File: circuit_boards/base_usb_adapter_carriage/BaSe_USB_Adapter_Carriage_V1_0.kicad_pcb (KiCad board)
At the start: 4 copper layers, 38.8 x 33.4 mm, 15 parts, among them J1 USB_C_Receptacle, J3 USB3_A, J4 Screw_Terminal_01x03, J5 Screw_Terminal_01x03, J6 Conn_01x03, J7 USB3_B_Micro, P1 USB_C_Plug

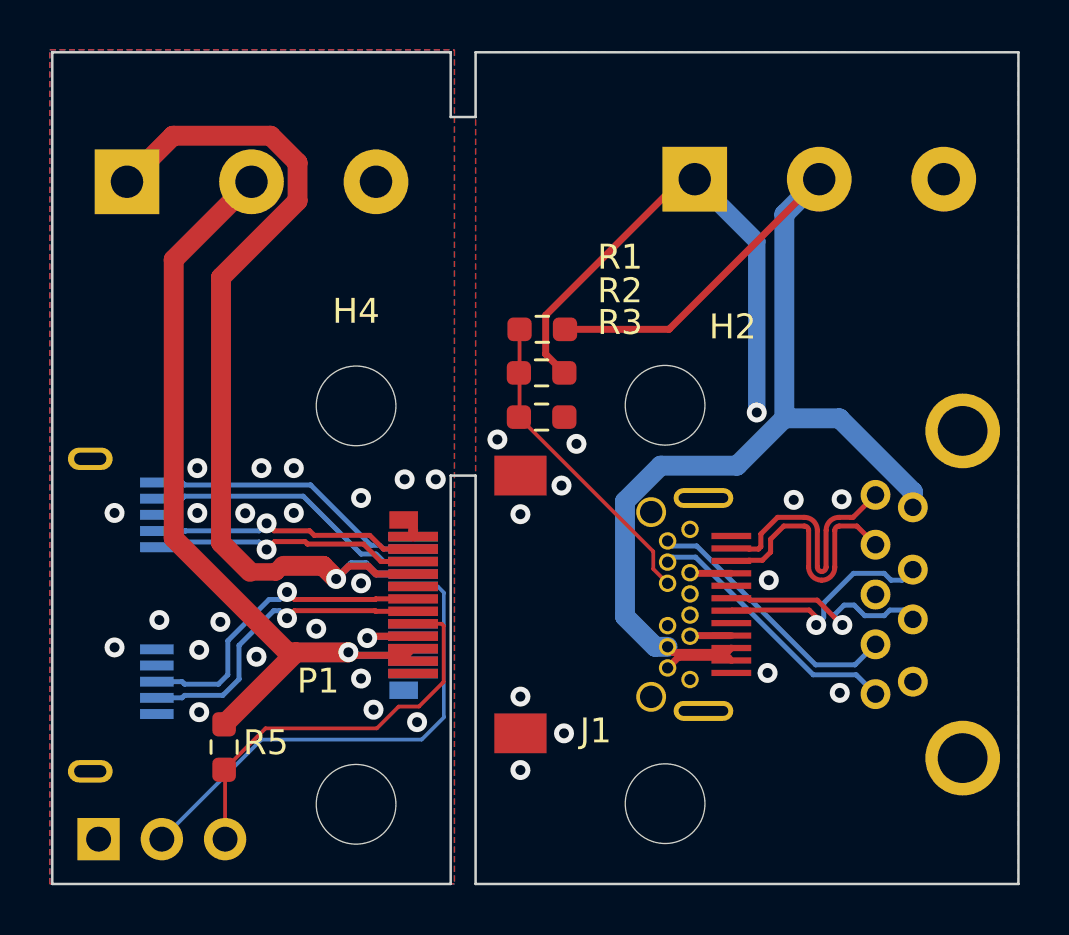
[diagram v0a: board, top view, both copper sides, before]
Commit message: shrinked hdd side part a little
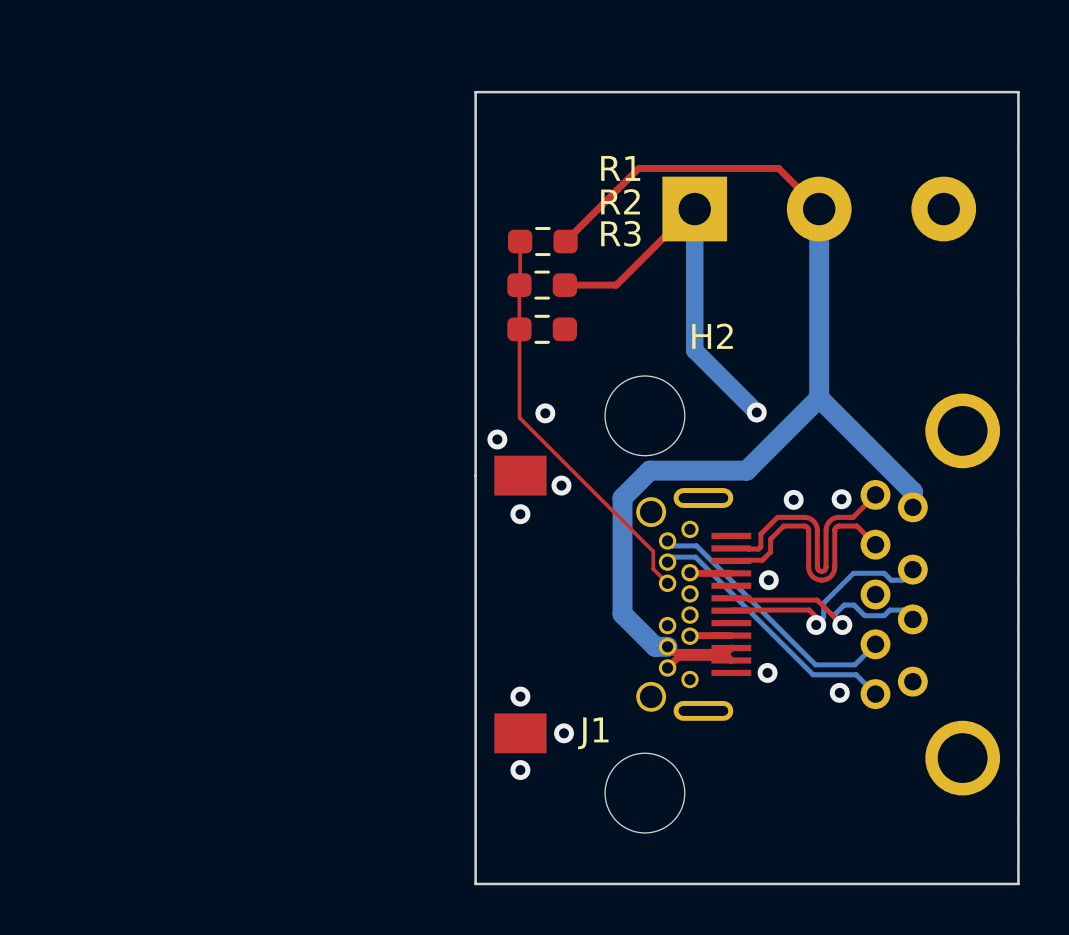
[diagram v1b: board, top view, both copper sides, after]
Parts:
- removed H3, H4: MountingHole, MountingHole:MountingHole_3.2mm_M3_DIN965
- removed J4: Screw_Terminal_01x03, TerminalBlock_Phoenix:TerminalBlock_Phoenix_MKDS-1,5-3_1x03_P5.00mm_Horizontal
- removed J6: Conn_01x03, Connector_PinHeader_2.54mm:PinHeader_1x03_P2.54mm_Vertical
- removed J7: USB3_B_Micro, g7_connectors:conn_usb3bmicro_GSB343K331HR
- removed P1: USB_C_Plug, g7_connectors:Molex_USBC_Plug_1054440011
- removed R5: 10k, Resistor_SMD:R_0603_1608Metric_Pad0.98x0.95mm_HandSolder
- moved R3 3.53 mm to (74.3, 73.7)
- moved R1 3.53 mm to (74.3, 70.2)
- moved R2 3.53 mm to (74.3, 72.0)
- moved J5 1.20 mm to (80.4, 68.9)
- moved H1 0.91 mm to (78.4, 92.3)
- moved H2 0.91 mm to (78.4, 77.2)
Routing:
- net +12VA: track 43.6 -> 0.00 mm, vias 2 -> 0
- net +5VA: track 34.1 -> 0.00 mm, vias 1 -> 0
- net /stator_supply_sense: track 19.7 -> 0.00 mm
- net /stator_docked_sense: track 16.6 -> 0.00 mm
- net /stator_d+: track 12.8 -> 0.00 mm, vias 1 -> 0
- net /stator_d-: track 12.8 -> 0.00 mm, vias 1 -> 0
- net /stator_rx-: track 11.4 -> 0.00 mm
- net /stator_rx+: track 11.4 -> 0.00 mm
- net /stator_tx-: track 11.0 -> 0.00 mm, vias 1 -> 0
- net /stator_tx+: track 10.8 -> 0.00 mm, vias 1 -> 0
- net +12V: track 36.3 -> 30.7 mm
- net /supply_sense: track 12.7 -> 16.2 mm
- net +5V: track 50.9 -> 48.6 mm
- net GND1: track 0.29 -> 0.00 mm, vias 21 -> 0
- removed copper zone on B.Cu, net GND1
- removed copper zone on F.Cu, net GND1
- removed copper zone on In1.Cu, net GND1
- removed copper zone on In2.Cu, net GND1
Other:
- board size 38.8 x 33.4 mm -> 21.8 x 31.8 mm
